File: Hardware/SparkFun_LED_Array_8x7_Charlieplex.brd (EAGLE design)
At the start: 27.9 x 43.2 mm, 73 parts

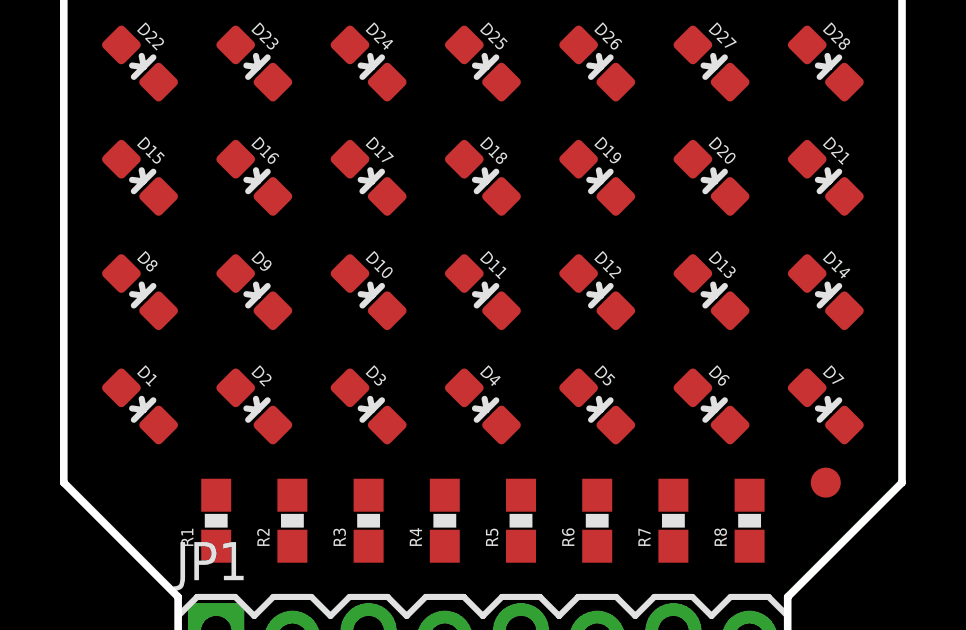
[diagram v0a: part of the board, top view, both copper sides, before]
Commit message: Started layout
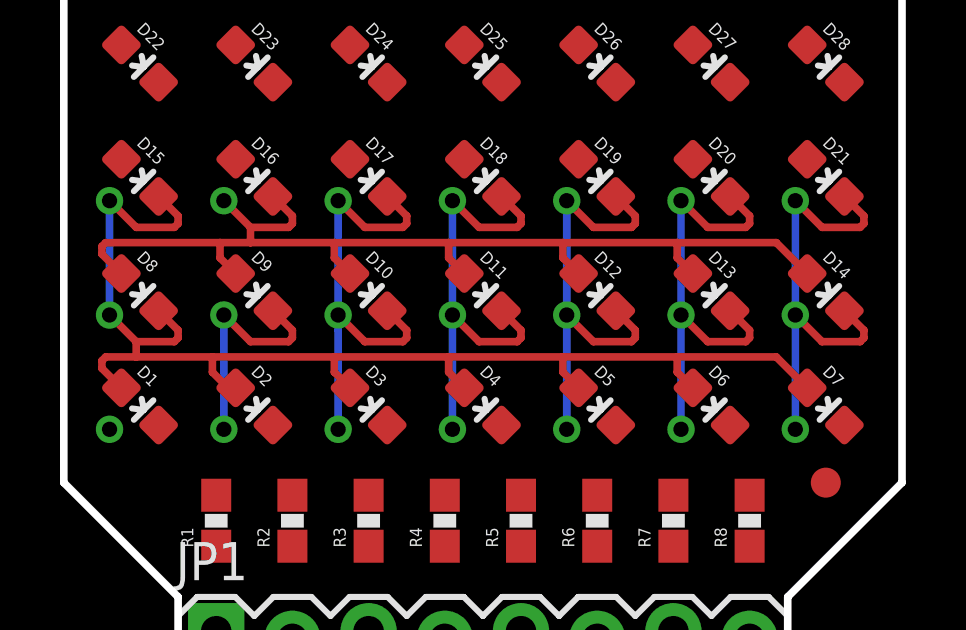
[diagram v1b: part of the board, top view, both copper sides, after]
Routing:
- net P1: track 0.00 -> 43.7 mm, vias 0 -> 2
- net P2: track 0.00 -> 35.8 mm, vias 0 -> 2
- net P8: track 0.00 -> 15.4 mm, vias 0 -> 3
- net P6: track 0.00 -> 15.4 mm, vias 0 -> 3
- net P4: track 0.00 -> 15.4 mm, vias 0 -> 3
- net P7: track 0.00 -> 15.4 mm, vias 0 -> 3
- net P5: track 0.00 -> 15.4 mm, vias 0 -> 3
- net P3: track 0.00 -> 7.69 mm, vias 0 -> 2

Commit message: Layout complete.
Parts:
- FRAME1: value FRAME-LETTER -> (none)
- JP1: device SparkFun-Connectors:1X08_LOCK -> SparkFun-Connectors:1X08_LOCK_NO_SILK
- moved LOGO2 20.3 mm to (26.2, 36.1), flipped to the bottom, turned to 270 degrees
- moved JP1 17.8 mm to (22.9, 1.27), turned to 180 degrees
- moved LOGO1 17.6 mm to (27.7, 23.1), flipped to the bottom, turned to 270 degrees
- moved FID2 1.42 mm to (6.35, 38.7)
- moved FID1 0.90 mm to (24.8, 5.71)
- moved U$1 0.25 mm to (8.00, 37.3)
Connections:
- net N$1: now also JP1.4; no longer JP1.5
- net N$2: now also JP1.5; no longer JP1.4
- net N$3: now also JP1.6; no longer JP1.3
- net N$4: now also JP1.7; no longer JP1.2
- net N$5: now also JP1.8; no longer JP1.1
- net N$6: now also JP1.3; no longer JP1.6
- net N$7: now also JP1.2; no longer JP1.7
- net N$8: now also JP1.1; no longer JP1.8
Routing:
- net P3: track 7.69 -> 90.5 mm, vias 2 -> 7
- net P8: track 15.4 -> 91.5 mm, vias 3 -> 8
- net P7: track 15.4 -> 90.3 mm, vias 3 -> 7
- net P4: track 15.4 -> 89.8 mm, vias 3 -> 7
- net P5: track 15.4 -> 88.7 mm, vias 3 -> 7
- net P6: track 15.4 -> 88.6 mm, vias 3 -> 7
- net P2: track 35.8 -> 97.5 mm, vias 2 -> 7
- net P1: track 43.7 -> 90.8 mm, vias 2 -> 8
- net N$8: track 0.00 -> 3.09 mm
- net N$6: track 0.00 -> 3.09 mm
- net N$4: track 0.00 -> 3.09 mm
- net N$2: track 0.00 -> 3.09 mm
- net N$7: track 0.00 -> 2.83 mm
- net N$5: track 0.00 -> 2.83 mm
- net N$3: track 0.00 -> 2.83 mm
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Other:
- board text added: "2"
- board text added: "3"
- board text added: "4"
- board text added: "5"
- board text added: "6"
- board text added: "7"
- board text added: "8"
- board text added: "9"
- board text added: "sparkfun.com/badgerhack"
